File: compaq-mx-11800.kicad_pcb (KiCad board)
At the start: 2 copper layers, 389.5 x 166.4 mm, 245 parts, among them J1 Conn_01x16_Female, J2 Conn_01x16_Female, j1 MX-NoLED, k1 MX-NoLED, m1 MX-NoLED, p1 MX-NoLED, q1 MX-NoLED, t1 MX-NoLED, u1 MX-NoLED, x1 MX-NoLED, y1 MX-NoLED

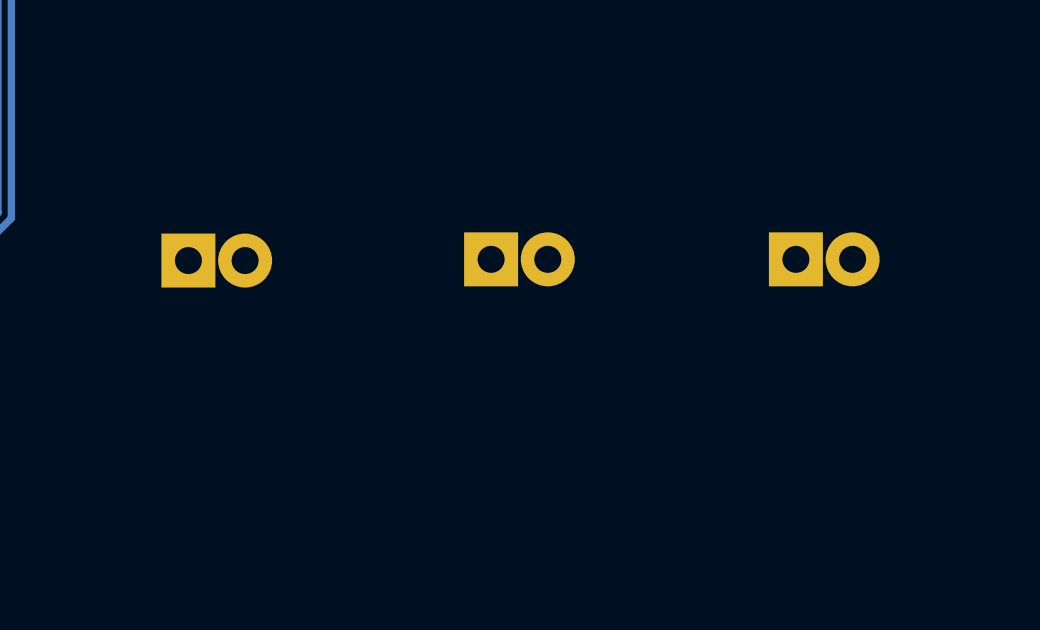
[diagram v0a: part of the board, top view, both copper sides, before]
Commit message: add polarity markings for LEDS
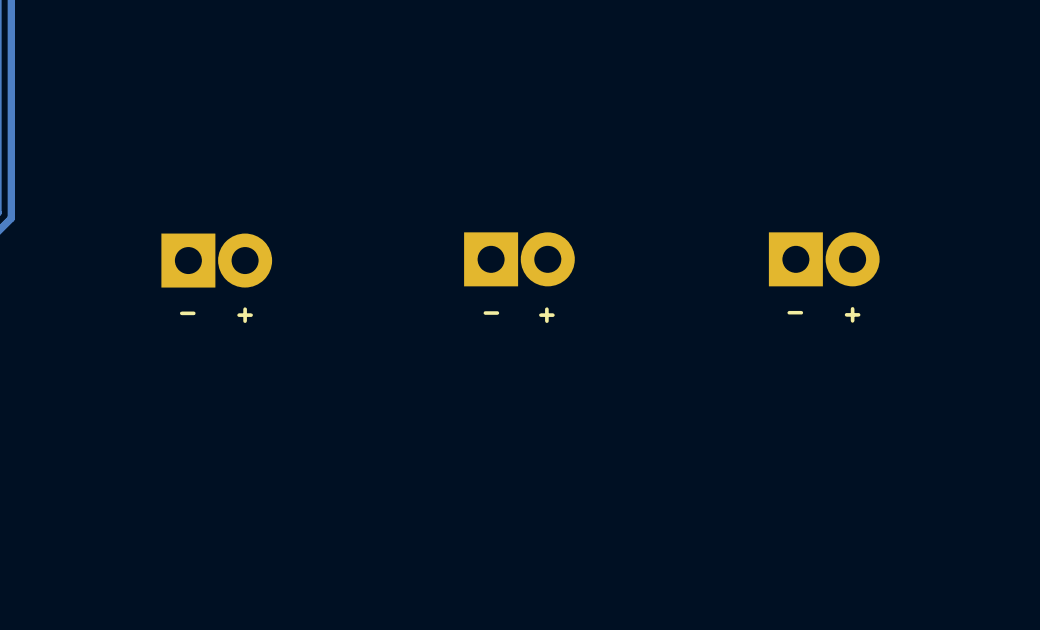
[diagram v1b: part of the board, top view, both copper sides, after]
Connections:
- net col9 renamed Net-(J2-Pad11)

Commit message: modify bottom row
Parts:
- removed MXextra_mod2, left_alt2, left_ctrl2: MX-NoLED, MX_Only:MXOnly-1U-NoLED
- removed extra_mod1, right_alt2, right_ctrl2: MX-NoLED, MX_Only:MXOnly-1.25U-NoLED
- removed right_alt1, right_ctrl1: MX-NoLED, MX_Only:MXOnly-1.5U-NoLED
- added D75: D_Small, Keebio-Parts:Diode-dual, B.Cu at (95.3, 214.1)
- added L_mod1_alt1: MX-NoLED, MX_Alps_Hybrid:MX-1.25U-NoLED, F.Cu at (31.0, 212.4)
- added L_mod2_alt1: MX-NoLED, MX_Alps_Hybrid:MX-1.25U-NoLED, F.Cu at (54.8, 212.4)
- added L_mod3: MX-NoLED, MX_Alps_Hybrid:MX-1.25U-NoLED, F.Cu at (78.6, 212.4)
- added R_mod1: MX-NoLED, MX_Alps_Hybrid:MX-1.25U-NoLED, F.Cu at (207.2, 212.4)
- added R_mod2: MX-NoLED, MX_Alps_Hybrid:MX-1.5U-NoLED, F.Cu at (223.8, 212.4)
- added R_mod2_alt1: MX-NoLED, MX_Alps_Hybrid:MX-1.25U-NoLED, F.Cu at (231.0, 212.4)
- added R_mod3: MX-NoLED, MX_Alps_Hybrid:MX-1.5U-NoLED, F.Cu at (252.4, 212.4)
- added R_mod3_alt1: MX-NoLED, MX_Alps_Hybrid:MX-1.25U-NoLED, F.Cu at (250.0, 212.4)
- L_mod1: renamed from left_ctrl1; footprint MX_Only:MXOnly-1.5U-NoLED -> MX_Alps_Hybrid:MX-1.5U-NoLED
- L_mod2: renamed from left_alt1; footprint MX_Only:MXOnly-1.5U-NoLED -> MX_Alps_Hybrid:MX-1.5U-NoLED
- space1: footprint MX_Only:MXOnly-7U-NoLED -> MX_Alps_Hybrid:MX-7U-NoLED
- space2: footprint MX_Only:MXOnly-7U-NoLED -> MX_Alps_Hybrid:MX-6.25U-NoLED
- space3: footprint MX_Only:MXOnly-6.25U-NoLED -> MX_Alps_Hybrid:MX-6.25U-NoLED
- moved space2 2.38 mm to (150.0, 212.4)
- moved D122 1.26 mm to (70.3, 214.1)
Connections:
- space1 pad 1: col0 -> Net-(D120-Pad2)
- space1 pad 2: Net-(D120-Pad2) -> col0
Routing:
- net col6: track 576.2 -> 533.9 mm
- net col0: track 602.6 -> 560.7 mm
- net Net-(D118-Pad2): track 52.0 -> 16.9 mm
- net col5: track 443.4 -> 423.2 mm
- net Net-(D117-Pad2): track 32.5 -> 16.7 mm
- net Net-(D75-Pad2): track 0.00 -> 15.2 mm
- net row12: track 782.2 -> 797.0 mm
- net col2: track 768.8 -> 778.9 mm
- net Net-(D121-Pad2): track 16.1 -> 23.5 mm
- net Net-(D124-Pad2): track 16.9 -> 21.5 mm
- net Net-(D120-Pad2): track 24.3 -> 28.3 mm
- net row13: track 837.3 -> 841.2 mm
- net Net-(D122-Pad2): track 22.7 -> 25.5 mm
- net col3: track 912.3 -> 912.8 mm
- removed copper zone on B.Cu, net (none)
- removed copper zone on F.Cu, net (none)
- removed copper zone on F.Cu, net GND
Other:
- board text removed: "10u"

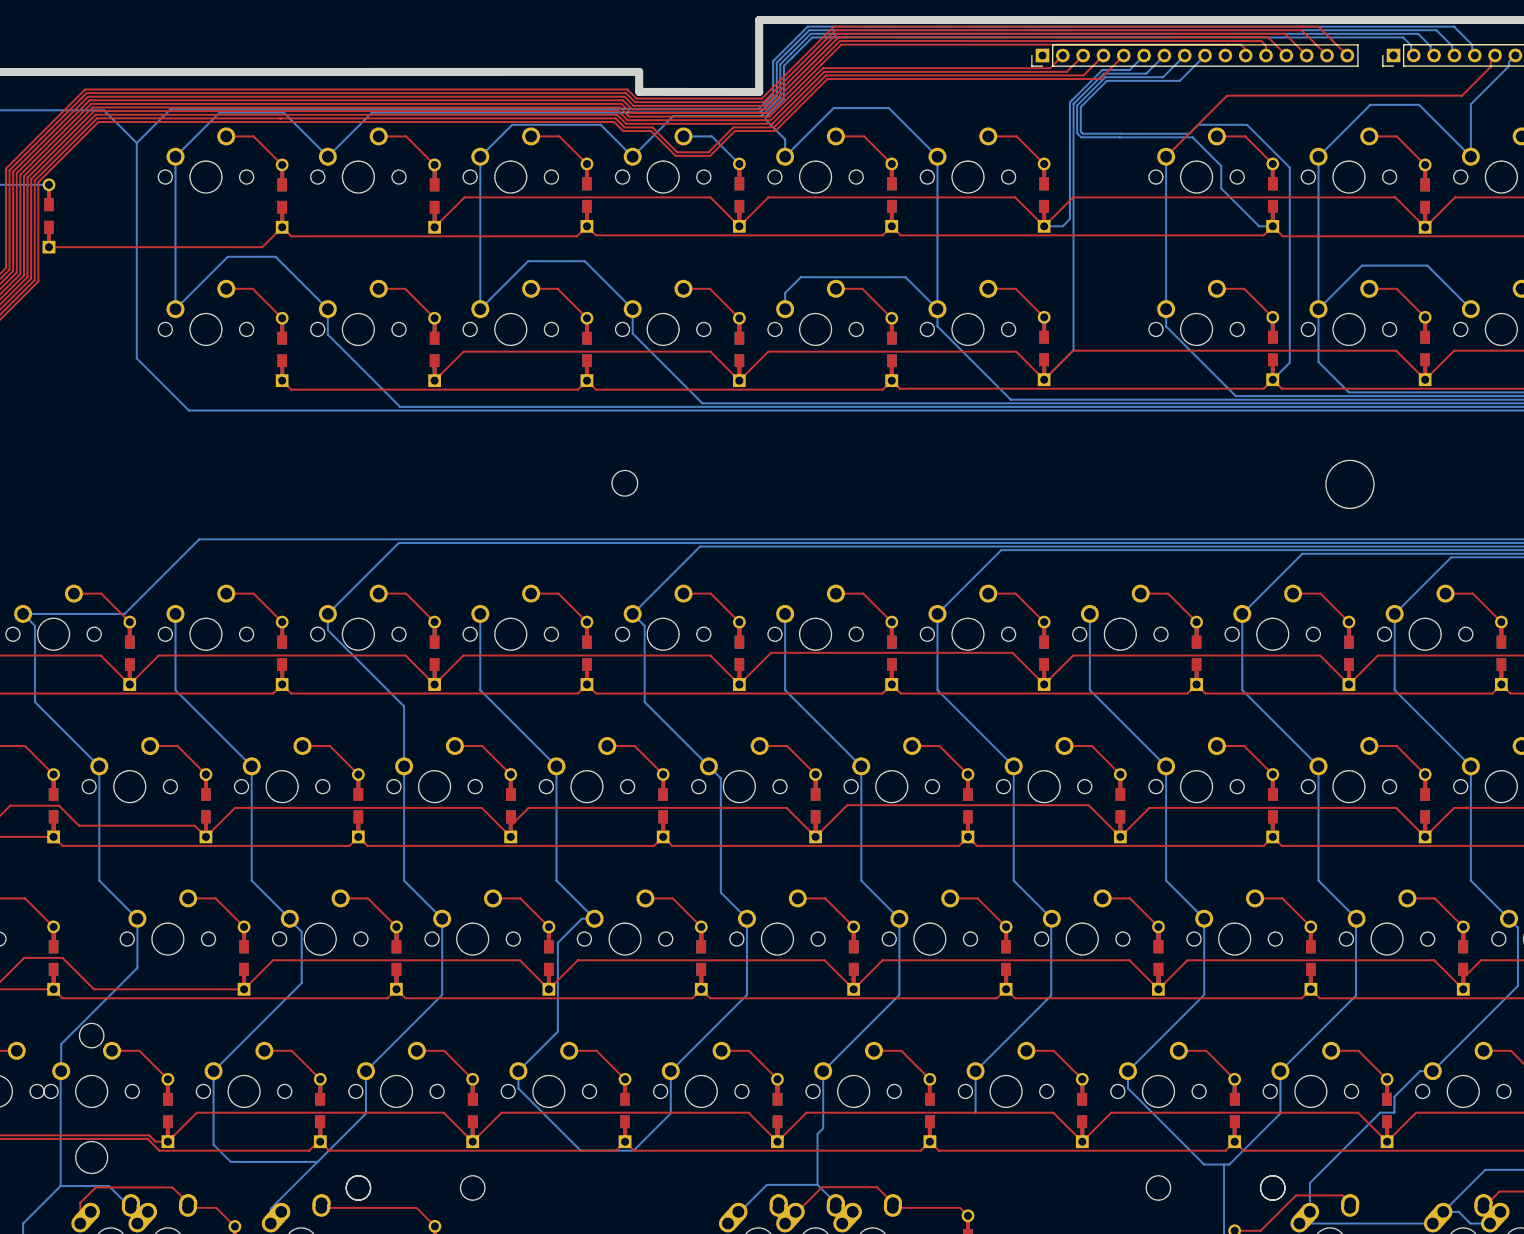
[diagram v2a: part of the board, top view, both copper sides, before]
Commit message: reorder columns and rows in schema and pcb to be in order
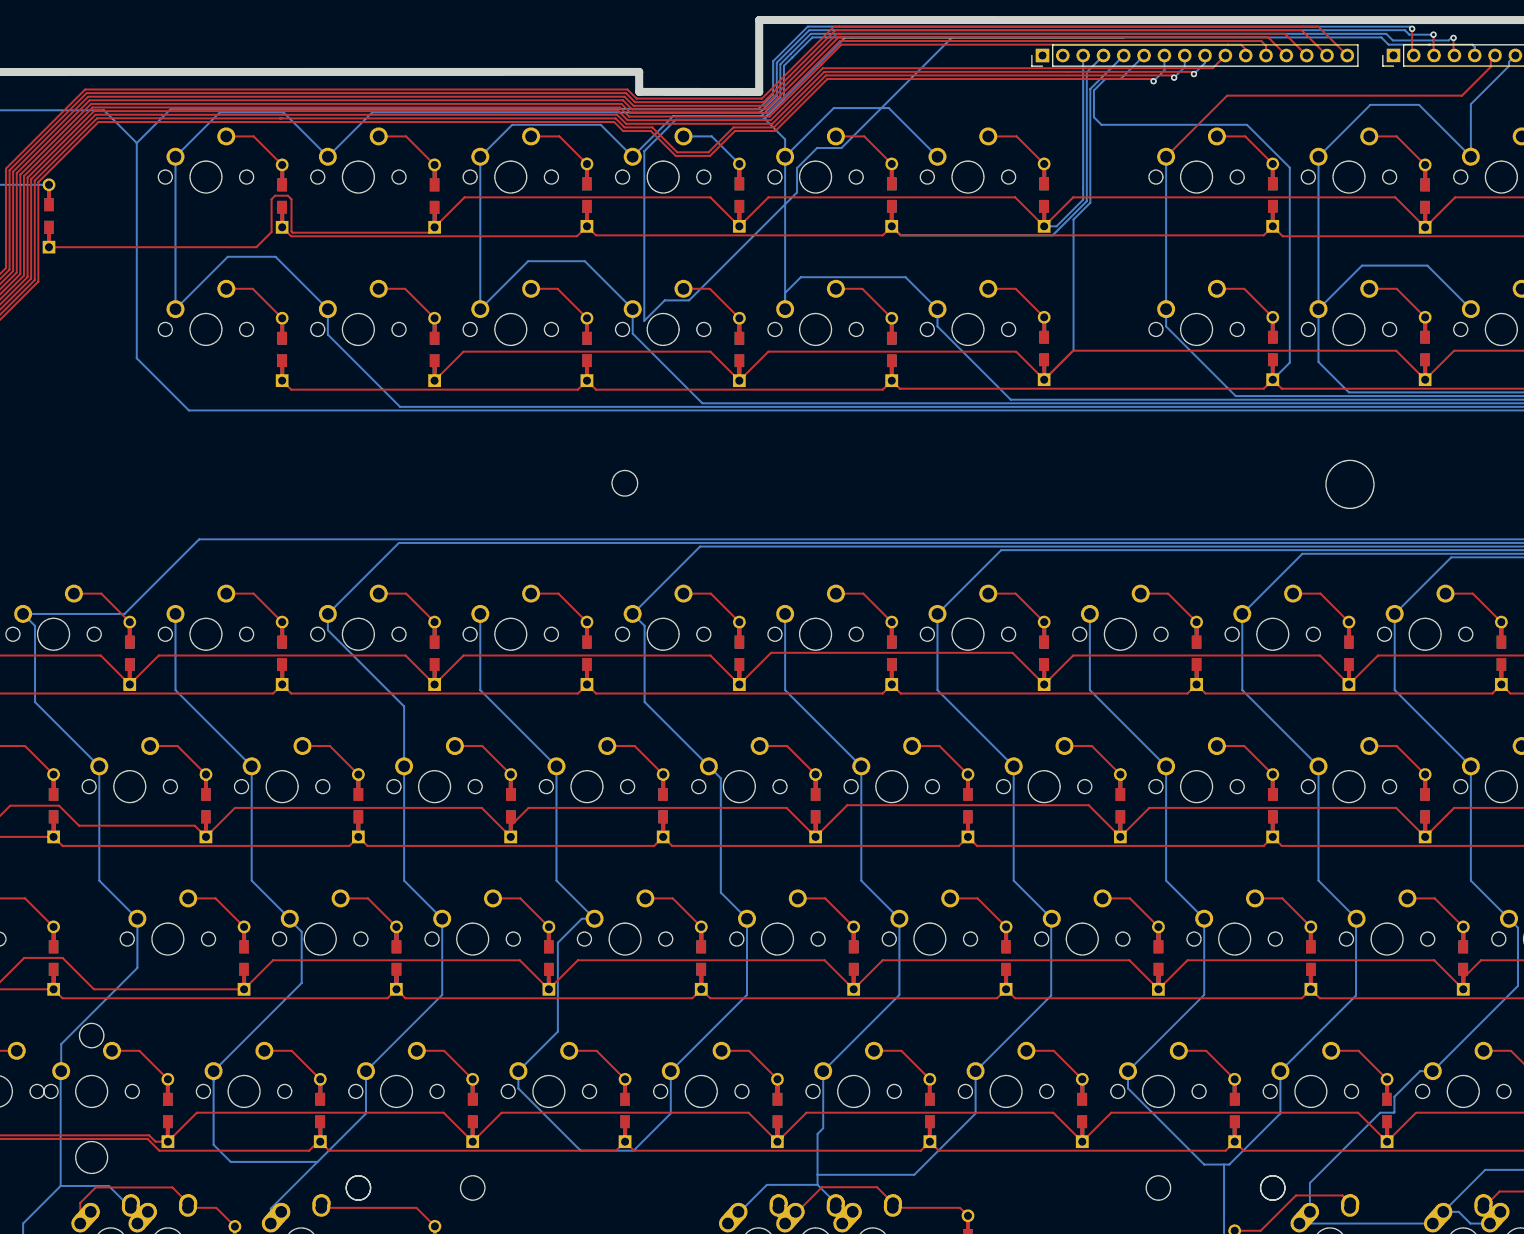
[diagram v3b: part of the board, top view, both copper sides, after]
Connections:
- D1 pad 1: row6 -> row0
- D10 pad 1: row6 -> row1
- D11 pad 1: row4 -> row0
- D12 pad 1: row6 -> row1
- D13 pad 1: row6 -> row1
- D14 pad 1: row4 -> row0
- D15 pad 1: row6 -> row1
- D16 pad 1: row4 -> row0
- D18 pad 1: row7 -> row3
- D19 pad 1: row5 -> row2
- D2 pad 1: row6 -> row1
- D20 pad 1: row7 -> row3
- D21 pad 1: row5 -> row2
- D22 pad 1: row7 -> row3
- D23 pad 1: row5 -> row2
- D24 pad 1: row7 -> row3
- D25 pad 1: row5 -> row2
- D26 pad 1: row7 -> row3
- D27 pad 1: row7 -> row3
- D28 pad 1: row7 -> row3
- D29 pad 1: row5 -> row2
- D3 pad 1: row4 -> row0
- D30 pad 1: row7 -> row3
- D31 pad 1: row3 -> row4
- D32 pad 1: row5 -> row2
- D33 pad 1: row0 -> row7
- D34 pad 1: row2 -> row5
- D35 pad 1: row3 -> row4
- D36 pad 1: row1 -> row6
- D37 pad 1: row2 -> row5
- D38 pad 1: row3 -> row4
- D39 pad 1: row2 -> row5
- D4 pad 1: row6 -> row1
- D40 pad 1: row3 -> row4
- D41 pad 1: row2 -> row5
- D42 pad 1: row3 -> row4
- D43 pad 1: row2 -> row5
- D44 pad 1: row3 -> row4
- D45 pad 1: row2 -> row5
- D46 pad 1: row3 -> row4
- D47 pad 1: row2 -> row5
- D48 pad 1: row3 -> row4
- D49 pad 1: row2 -> row5
- D5 pad 1: row4 -> row0
- D51 pad 1: row2 -> row5
- D58 pad 1: row0 -> row7
- D59 pad 1: row1 -> row6
- D6 pad 1: row6 -> row1
- D60 pad 1: row0 -> row7
- D61 pad 1: row1 -> row6
- D62 pad 1: row0 -> row7
- D63 pad 1: row1 -> row6
- D64 pad 1: row0 -> row7
- D65 pad 1: row1 -> row6
- D66 pad 1: row0 -> row7
- D67 pad 1: row1 -> row6
- D68 pad 1: row0 -> row7
- D69 pad 1: row1 -> row6
- D7 pad 1: row4 -> row0
- D70 pad 1: row0 -> row7
- D71 pad 1: row1 -> row6
- D8 pad 1: row6 -> row1
- D9 pad 1: row4 -> row0
- J1 pad 10: Net-(J1-Pad10) -> row7
- J1 pad 2: row0 -> Net-(J1-Pad2)
- J1 pad 3: row1 -> row0
- J1 pad 4: row2 -> row1
- J1 pad 5: row3 -> row2
- J1 pad 6: row4 -> row3
- J1 pad 7: row5 -> row4
- J1 pad 8: row6 -> row5
- J1 pad 9: row7 -> row6
- L_mod1 pad 1: col3 -> col0
- L_mod1_alt1 pad 1: col3 -> col0
- L_mod2 pad 1: col3 -> col0
- L_mod2_alt1 pad 2: col3 -> col0
- L_mod3 pad 1: col2 -> col1
- NUBS1 pad 1: col3 -> col0
- a1 pad 1: col3 -> col0
- b1 pad 1: col0 -> col3
- c1 pad 1: col1 -> col2
- capslock1 pad 1: col3 -> col0
- d1 pad 1: col2 -> col1
- e1 pad 1: col2 -> col1
- escape1 pad 1: col3 -> col0
- f1 pad 1: col2 -> col1
- f10 pad 1: col1 -> col2
- f11 pad 1: col0 -> col3
- f12 pad 1: col0 -> col3
- f13 pad 1: col1 -> col2
- f2 pad 1: col2 -> col1
- f3 pad 1: col1 -> col2
- f4 pad 1: col1 -> col2
- f5 pad 1: col0 -> col3
- f6 pad 1: col0 -> col3
- f7 pad 1: col2 -> col1
- f8 pad 1: col2 -> col1
- f9 pad 1: col1 -> col2
- g1 pad 1: col1 -> col2
- grave1 pad 1: col3 -> col0
- h1 pad 1: col0 -> col3
- j1 pad 1: col0 -> col3
- left_shift1 pad 1: col3 -> col0
- left_shift2 pad 1: col3 -> col0
- n1 pad 1: col3 -> col0
- n10 pad 1: col0 -> col3
- n2 pad 1: col2 -> col1
- n3 pad 1: col2 -> col1
- n4 pad 1: col1 -> col2
- n5 pad 1: col1 -> col2
- n6 pad 1: col0 -> col3
- n7 pad 1: col0 -> col3
- q1 pad 1: col3 -> col0
- r1 pad 1: col1 -> col2
- s1 pad 1: col2 -> col1
- space1 pad 2: col0 -> col3
- space2 pad 1: col0 -> col3
- space3 pad 1: col0 -> col3
- stepped_capslock1 pad 1: col3 -> col0
- t1 pad 1: col1 -> col2
- tab1 pad 1: col3 -> col0
- u1 pad 1: col0 -> col3
- v1 pad 1: col1 -> col2
- w1 pad 1: col2 -> col1
- x1 pad 1: col2 -> col1
- y1 pad 1: col0 -> col3
- z1 pad 1: col2 -> col1
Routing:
- net col0: track 560.7 -> 906.8 mm, vias 0 -> 1
- net row7: track 395.7 -> 723.8 mm
- net row3: track 711.0 -> 384.0 mm
- net row5: track 388.9 -> 664.7 mm, vias 0 -> 1
- net row1: track 712.3 -> 440.1 mm
- net row2: track 653.4 -> 383.7 mm
- net row4: track 448.9 -> 717.4 mm, vias 0 -> 1
- net row6: track 475.0 -> 728.3 mm, vias 0 -> 1
- net row0: track 703.4 -> 502.5 mm
- net col3: track 912.8 -> 733.9 mm
- net col1: track 643.8 -> 777.9 mm, vias 0 -> 1
- net col2: track 778.9 -> 648.0 mm, vias 0 -> 1

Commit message: revert to using MX_only
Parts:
- L_mod1, L_mod2, R_mod2, R_mod3: footprint MX_Alps_Hybrid:MX-1.5U-NoLED -> MX_Only:MXOnly-1.5U-NoLED
- L_mod1_alt1, L_mod2_alt1, L_mod3, R_mod1, R_mod2_alt1, R_mod3_alt1: footprint MX_Alps_Hybrid:MX-1.25U-NoLED -> MX_Only:MXOnly-1.25U-NoLED
- space1: footprint MX_Alps_Hybrid:MX-7U-NoLED -> MX_Only:MXOnly-7U-NoLED
- space2, space3: footprint MX_Alps_Hybrid:MX-6.25U-NoLED -> MX_Only:MXOnly-6.25U-NoLED
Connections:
- L_mod2_alt1 pad 1: Net-(D122-Pad2) -> col0
- L_mod2_alt1 pad 2: col0 -> Net-(D122-Pad2)
- space1 pad 1: Net-(D120-Pad2) -> col3
- space1 pad 2: col3 -> Net-(D120-Pad2)
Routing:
- net Net-(D122-Pad2): track 25.5 -> 15.1 mm
- net col3: track 733.9 -> 739.9 mm
- net Net-(D120-Pad2): track 28.3 -> 24.3 mm
- net Net-(D124-Pad2): track 21.5 -> 18.9 mm
- net col5: track 423.2 -> 425.2 mm

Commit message: remove solder mask from front pcb traces
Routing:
- net row10: track 759.8 -> 761.8 mm
- net Net-(D122-Pad2): track 15.1 -> 14.2 mm

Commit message: update diode footprint
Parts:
- D10, D100, D101, D102, D103, D104, D105, D107, D108, D11, D114, D115, D116, D117, D118, D12, D120, D121, D122, D124, D13, D14, D15, D16, D18, D19, D2, D20, D21, D22, D23, D24, D25, D26, D27, D28, D29, D3, D30, D31, D32, D33, D34, D35, D36, D37, D38, D39, D4, D40, D41, D42, D43, D44, D45, D46, D47, D48, D49, D5, D51, D53, D54, D55, D56, D57, D58, D59, D6, D60, D61, D62, D63, D64, D65, D66, D67, D68, D69, D7, D70, D71, D72, D73, D74, D75, D76, D77, D78, D79, D8, D80, D81, D82, D83, D84, D85, D86, D87, D88, D9, D91, D92, D94, D95, D96, D97, D98, D99: footprint Keebio-Parts:Diode-dual -> vuckale:Diode
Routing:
- net row0: track 502.5 -> 498.0 mm
- net row8: track 707.2 -> 707.8 mm

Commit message: add 1u-1u-1u-7u-1u-1u-1u support for bottom row
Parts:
- added L_mod1_1U1: MX-NoLED, MX_Only:MXOnly-1U-NoLED, F.Cu at (28.6, 212.4)
- added L_mod2_1U1: MX-NoLED, MX_Only:MXOnly-1U-NoLED, F.Cu at (47.6, 212.4)
- added L_mod3_1U1: MX-NoLED, MX_Only:MXOnly-1U-NoLED, F.Cu at (66.7, 212.4)
- added R_mod1_1U1: MX-NoLED, MX_Only:MXOnly-1U-NoLED, F.Cu at (219.1, 212.4)
- added R_mod2_1U1: MX-NoLED, MX_Only:MXOnly-1U-NoLED, F.Cu at (238.1, 212.4)
- added R_mod3_1U1: MX-NoLED, MX_Only:MXOnly-1U-NoLED, F.Cu at (257.2, 212.4)
- moved D122 21.9 mm to (92.2, 214.1)
- moved D118 8.18 mm to (244.6, 221.9), turned to 0 degrees
- moved D124 7.48 mm to (271.5, 216.9)
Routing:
- net Net-(D122-Pad2): track 14.2 -> 48.9 mm
- net col1: track 777.9 -> 790.5 mm
- net Net-(D118-Pad2): track 16.9 -> 28.8 mm
- net Net-(D75-Pad2): track 15.2 -> 27.1 mm
- net Net-(D117-Pad2): track 16.7 -> 27.8 mm
- net col0: track 906.9 -> 916.5 mm
- net col5: track 425.2 -> 431.9 mm
- net col6: track 533.9 -> 540.5 mm
- net Net-(D124-Pad2): track 18.9 -> 21.3 mm
- net row13: track 841.2 -> 839.2 mm
- net row6: track 728.3 -> 728.9 mm

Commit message: remove solder from traces on back PCB
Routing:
- net col3: track 739.9 -> 598.0 mm
- net row4: track 717.4 -> 697.5 mm
- net row0: track 498.0 -> 507.4 mm
- net row1: track 440.1 -> 448.9 mm
- net Net-(D31-Pad2): track 35.6 -> 31.7 mm
- net col7: track 598.3 -> 597.3 mm
